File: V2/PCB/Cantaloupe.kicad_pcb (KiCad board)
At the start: 2 copper layers, 143.9 x 118.7 mm, 121 parts, among them J1 USB_In, J2 OLED, J3 Link, J4 Debug, J5 Trackball, Q1 2N7002, Q2 AO3401A, SW1 MX, SW10 MX, SW11 MX, SW12 MX, SW13 MX, SW14 MX, SW15 MX, SW16 MX, SW17 MX, SW18 MX, SW19 MX, SW2 MX, SW20 MX, SW21 MX, SW22 MX, SW23 MX, SW24 MX, SW25 MX, SW26 MX, SW27 MX, SW28 MX, SW29 MX, SW3 MX, SW30 MX, SW31 Encoder, SW32 MX, SW4 MX, SW5 MX, SW6 MX, SW7 MX, SW8 MX, SW9 MX, U1 STM32F4x1CxUx, U2 SRV0504, U3 SRV0504, U4 XC6206P332MR, U5 LMV321, Y1 8MHz

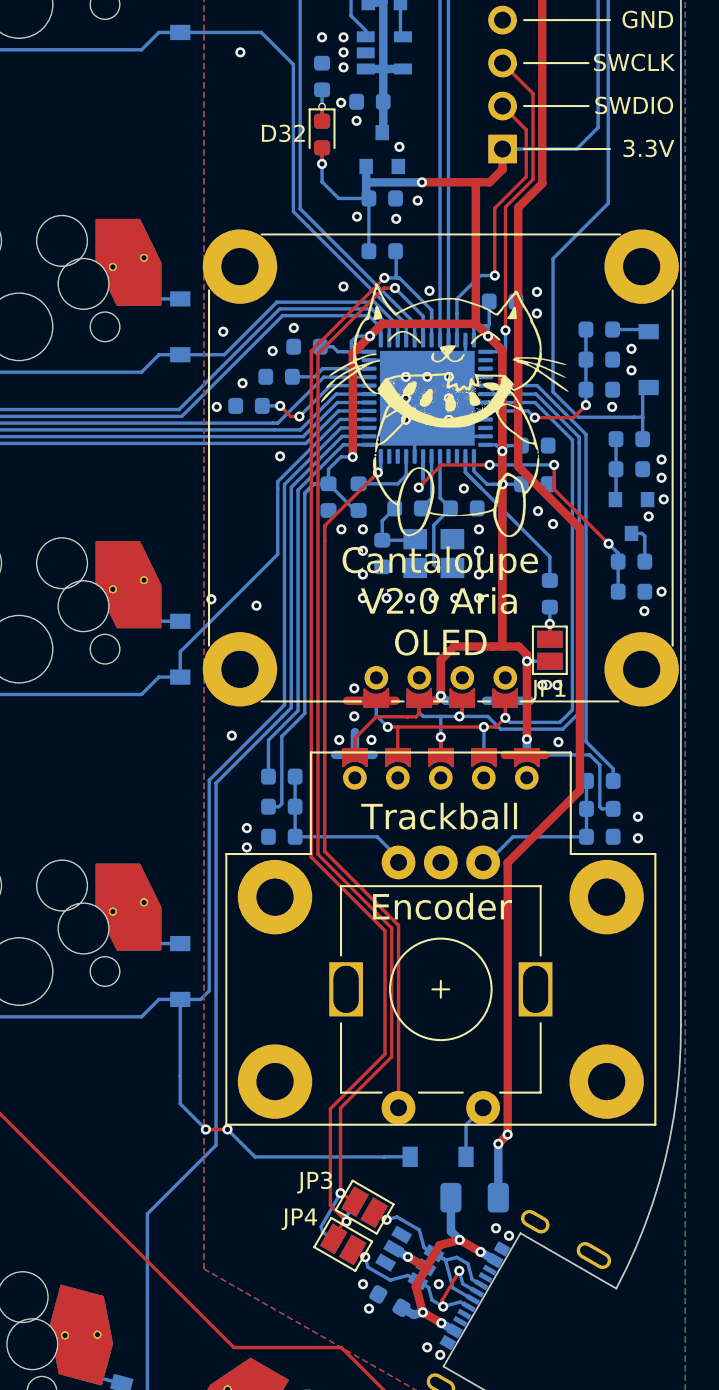
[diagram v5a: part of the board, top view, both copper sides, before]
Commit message: Update README.mdAdded silkscreen jumper guides. Connected indicator LED to spare GPIO. Updated images.
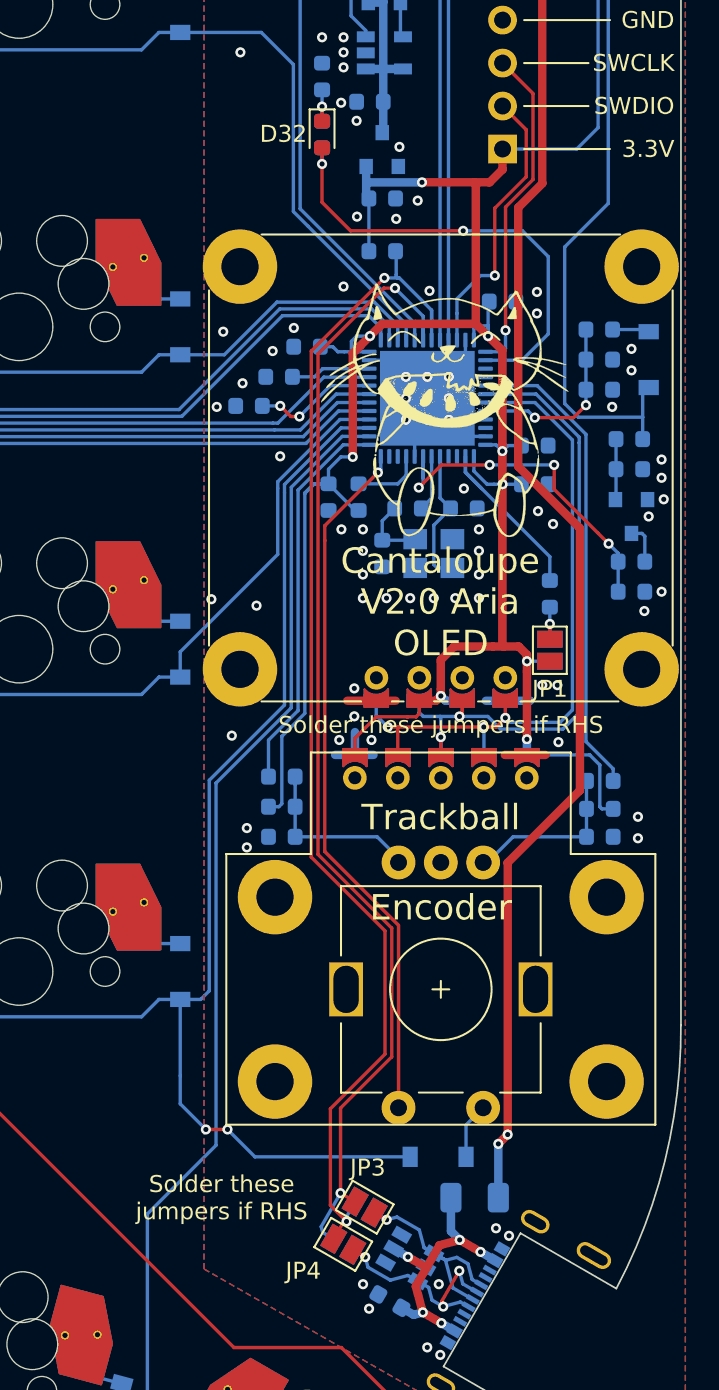
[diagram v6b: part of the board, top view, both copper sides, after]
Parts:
- JP1: value Side_L -> Side_R
- JP2: value Side_R -> Side_L
- JP3: value Link-_L -> Link-_R
- JP4: value Link+_L -> Link+_R
- JP5: value Link-_R -> Link-_L
- JP6: value Link+_R -> Link+_L
- R18: value 100k -> 10k
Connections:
- D32 pad 2: VDD -> LED
- J1 pad A8: Net-(J1-PadA8) -> unconnected-(J1-PadA8)
- J1 pad B8: Net-(J1-PadB8) -> unconnected-(J1-PadB8)
- J3 pad A5: Net-(J3-PadA5) -> unconnected-(J3-PadA5)
- J3 pad A8: Net-(J3-PadA8) -> unconnected-(J3-PadA8)
- J3 pad B5: Net-(J3-PadB5) -> unconnected-(J3-PadB5)
- J3 pad B8: Net-(J3-PadB8) -> unconnected-(J3-PadB8)
- U1 pad 10: Net-(U1-Pad10) -> unconnected-(U1-Pad10)
- U1 pad 11: Net-(U1-Pad11) -> unconnected-(U1-Pad11)
- U1 pad 3: Net-(U1-Pad3) -> unconnected-(U1-Pad3)
- U1 pad 38: Net-(U1-Pad38) -> LED
- U1 pad 39: Net-(U1-Pad39) -> unconnected-(U1-Pad39)
- U1 pad 4: Net-(U1-Pad4) -> unconnected-(U1-Pad4)
- U1 pad 40: Net-(U1-Pad40) -> unconnected-(U1-Pad40)
- U1 pad 45: Net-(U1-Pad45) -> unconnected-(U1-Pad45)
- U1 pad 46: Net-(U1-Pad46) -> unconnected-(U1-Pad46)
- U2 pad 4: Net-(U2-Pad4) -> unconnected-(U2-Pad4)
- U2 pad 6: Net-(U2-Pad6) -> unconnected-(U2-Pad6)
- U3 pad 4: Net-(U3-Pad4) -> unconnected-(U3-Pad4)
- U3 pad 6: Net-(U3-Pad6) -> unconnected-(U3-Pad6)
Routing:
- net LED: track 0.00 -> 27.9 mm, vias 0 -> 2
- net VDD: track 168.0 -> 162.4 mm, vias 11 -> 10
- net Net-(D33-Pad2): track 42.3 -> 41.8 mm
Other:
- board text added: "Solder these jumpers if LHS"
- board text added: "Solder these jumpers if RHS"

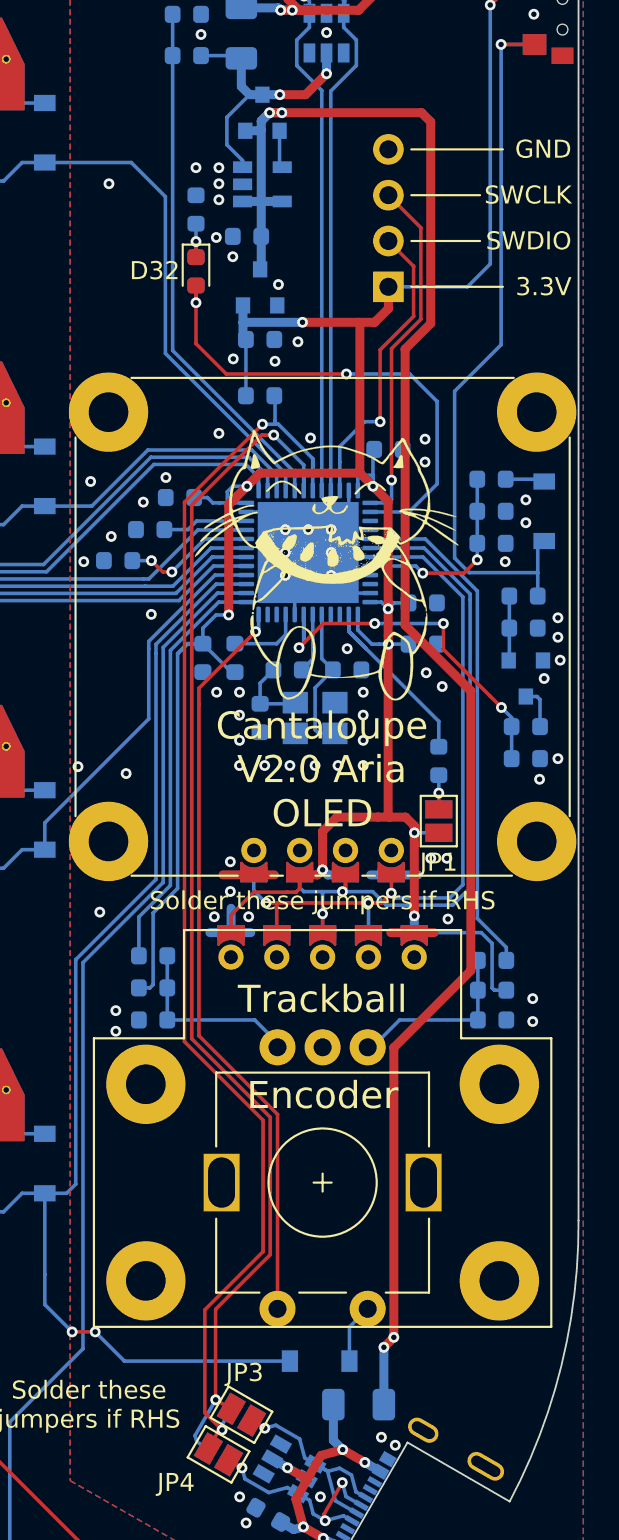
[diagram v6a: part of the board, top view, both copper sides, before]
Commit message: Update to PCB and case files, added cirque header, clean up of library
Added silkscreen jumper guides. Connected indicator LED to spare GPIO. Updated images. Added optional I2C resistors. New logo. New plate CAD files for potentiometer, trackball and trackpad options. Added header for Cirque trackpad. Cleaned up footprint library.
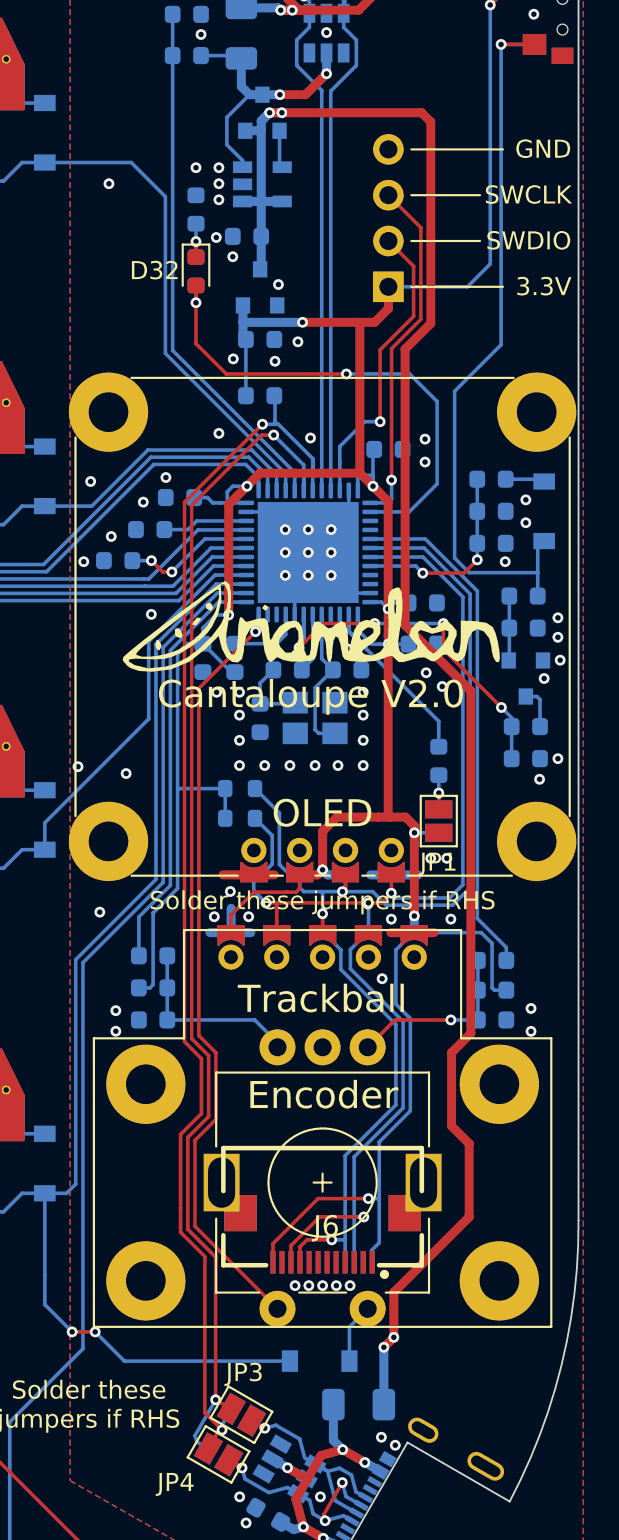
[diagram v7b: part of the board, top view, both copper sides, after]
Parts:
- added J6: Trackpad, Ariamelon:FPC-SMD_FPC05012-09200-.5mm-rev, F.Cu at (143.0, 91.6)
- added R19: 4.7k, Resistor_SMD:R_0603_1608Metric, B.Cu at (138.5, 66.7)
- added R20: 4.7k, Resistor_SMD:R_0603_1608Metric, B.Cu at (138.5, 68.3)
- A1: footprint Ariamelon:Catmelon -> Ariamelon:Ariamelon_Logo_x2
- moved A1 5.87 mm to (142.4, 57.7)
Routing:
- net VDD: track 162.4 -> 194.7 mm, vias 10 -> 11
- net SDA: track 39.6 -> 71.0 mm, vias 3 -> 4
- net SCL: track 38.9 -> 69.7 mm, vias 2 -> 3
- net RX: track 71.5 -> 69.8 mm
- net TX: track 67.9 -> 66.3 mm
- net COLROT: track 41.7 -> 42.6 mm
- net VBUS_In: track 97.6 -> 98.4 mm
- net Net-(C1-Pad2): vias 0 -> 1
- net GND: vias 88 -> 94
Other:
- board text added: "Cantaloupe V2.0"
- board text removed: "Cantaloupe V2.0 Aria"

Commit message: Update to V2.1
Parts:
- removed the J5 at (143.0, 88.5)
- J5: renamed from J6; footprint Ariamelon:FPC-SMD_FPC05012-09200-.5mm-rev -> Connector_FFC-FPC:Hirose_FH12-12S-0.5SH_1x12-1MP_P0.50mm_Horizontal
- moved J5 14.0 mm to (143.0, 77.6), turned to 0 degrees
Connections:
- J5 pad 1: unconnected-(J6-Pad1) -> VDD
- J5 pad 10: SDA -> unconnected-(J5-Pad10)
- J5 pad 11: GND -> unconnected-(J5-Pad11)
- J5 pad 12: VDD -> unconnected-(J5-Pad12)
- J5 pad 2: unconnected-(J6-Pad2) -> GND
- J5 pad 3: unconnected-(J6-Pad3) -> SDA
- J5 pad 4: unconnected-(J6-Pad4) -> SCL
- J5 pad 9: SCL -> unconnected-(J5-Pad9)
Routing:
- net SDA: track 71.0 -> 45.7 mm, vias 4 -> 3
- net VDD: track 194.7 -> 170.6 mm, vias 11 -> 10
- net SCL: track 69.7 -> 48.5 mm, vias 3 -> 2
- net GND: track 30.0 -> 13.2 mm, vias 94 -> 102
- net LED: track 27.9 -> 32.2 mm
- net Side: track 11.7 -> 9.40 mm
- net VBUS_In: track 98.4 -> 100.5 mm
- net COLROT: track 42.6 -> 44.4 mm
- net Net-(D33-Pad2): track 41.8 -> 40.4 mm
- net TX: track 66.3 -> 65.0 mm
- net Net-(D24-Pad2): track 2.81 -> 1.55 mm
- net Net-(D20-Pad2): track 2.81 -> 1.55 mm
- net Net-(D12-Pad2): track 2.81 -> 1.55 mm
- net Net-(D3-Pad2): track 2.81 -> 1.55 mm
- net Net-(D21-Pad2): track 2.81 -> 1.55 mm
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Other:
- outline, holes or cut-outs redrawn
- board text added: "Cantaloupe V2.1"
- board text added: "Trackpad"
- board text removed: "Cantaloupe V2.0"
- board text removed: "Solder these jumpers if LHS"
- board text removed: "Solder these jumpers if RHS"
- board text removed: "Trackball"
